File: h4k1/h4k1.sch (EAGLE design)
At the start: 159 parts, among them IC1 STM32F10XCXT6, K1 CHERRY-MX-LED, K10 CHERRY-MX-LED, K11 CHERRY-MX-LED, K12 CHERRY-MX-LED, K13 CHERRY-MX-LED, K14 CHERRY-MX-LED, K15 CHERRY-MX-LED, K16 CHERRY-MX-LED, K17 CHERRY-MX-LED, K18 CHERRY-MX-LED, K19 CHERRY-MX-LED, K2 CHERRY-MX-LED, K20 CHERRY-MX-LED, K21 CHERRY-MX-LED, K22 CHERRY-MX-LED, K23 CHERRY-MX-LED, K24 CHERRY-MX-LED, K25 CHERRY-MX-LED, K26 CHERRY-MX-LED, K27 CHERRY-MX-LED, K28 CHERRY-MX-LED, K29 CHERRY-MX-LED, K3 CHERRY-MX-LED, K30 CHERRY-MX-LED, K31 CHERRY-MX-LED, K32 CHERRY-MX-LED, K33 CHERRY-MX-LED, K34 CHERRY-MX-LED, K35 CHERRY-MX-LED, K36 CHERRY-MX-LED, K37 CHERRY-MX-LED, K38 CHERRY-MX-LED, K39 CHERRY-MX-LED, K4 CHERRY-MX-LED, K40 CHERRY-MX-LED, K41 CHERRY-MX-LED, K42 CHERRY-MX-LED, K43 CHERRY-MX-LED, K44 CHERRY-MX-LED, K45 CHERRY-MX-LED, K46 CHERRY-MX-LED, K47 CHERRY-MX-LED, K48 CHERRY-MX-LED, K49 CHERRY-MX-LED, K5 CHERRY-MX-LED, K50 CHERRY-MX-LED, K51 CHERRY-MX-LED, K52 CHERRY-MX-LED, K53 CHERRY-MX-LED, K54 CHERRY-MX-LED, K55 CHERRY-MX-LED, K56 CHERRY-MX-LED, K57 CHERRY-MX-LED, K58 CHERRY-MX-LED, K59 CHERRY-MX-LED, K6 CHERRY-MX-LED, K60 CHERRY-MX-LED, K61 CHERRY-MX-LED, K62 CHERRY-MX-LED, K63 CHERRY-MX-LED, K64 CHERRY-MX-LED, K7 CHERRY-MX-LED, K8 CHERRY-MX-LED, K9 CHERRY-MX-LED

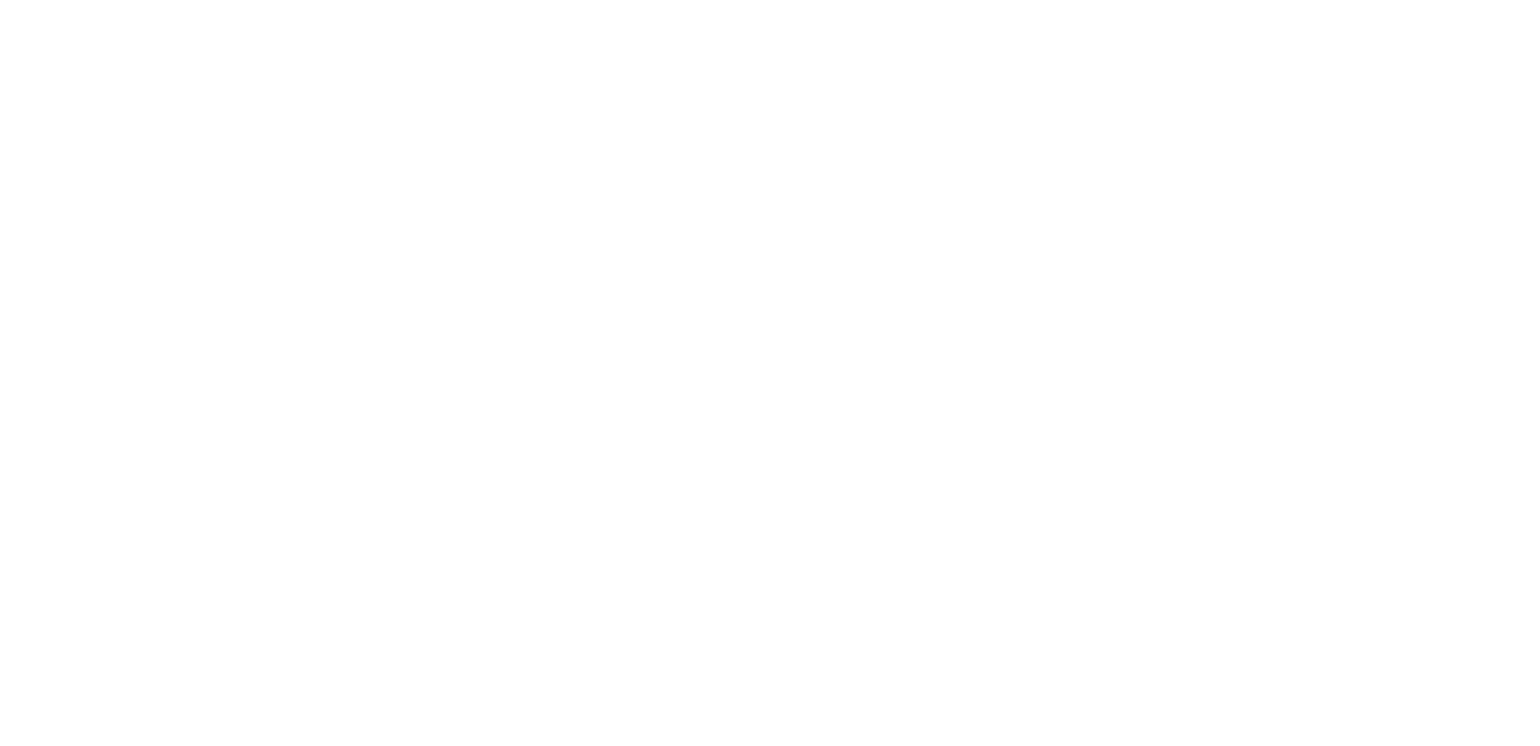
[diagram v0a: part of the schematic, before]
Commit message: add usb hub
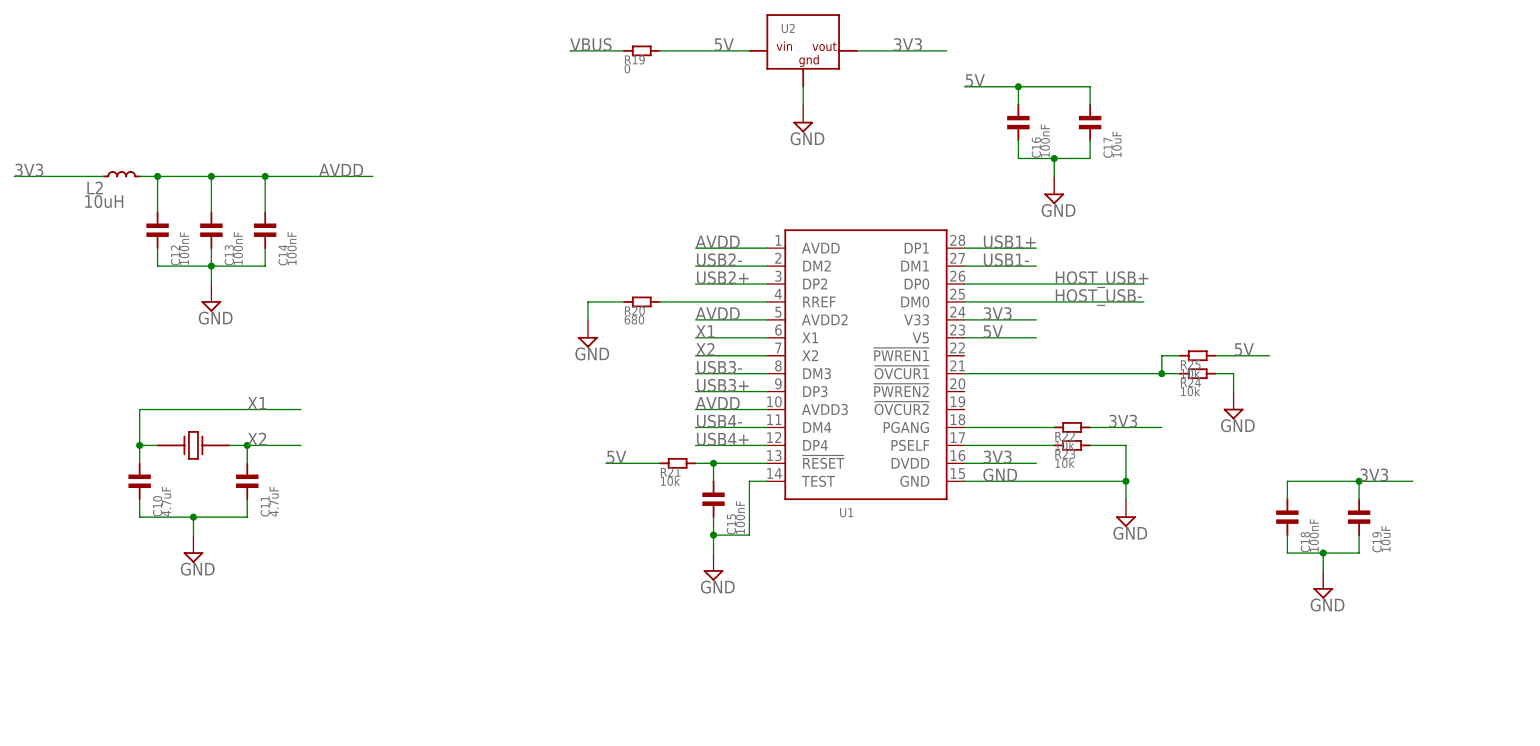
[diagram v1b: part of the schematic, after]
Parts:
- added C10, C11: 4.7uF, hqc-basic:C-0603
- added C12, C13, C14, C15, C16, C18: 100nF, hqc-basic:C-0603
- added C17, C19: 10uF, hqc-basic:C-0603
- added L2: 10uH, hqc-basic:L-0603
- added R19: 0, hqc-basic:R-0603
- added R20: 680, hqc-basic:R-0603
- added R21, R22, R23, R24, R25: 10k, hqc-basic:R-0603
- added U1: G850G, hqc-communication:G850G
- added U2: (no value), hqc-power:AMS1117-33
- added X3: (no value), hqc-crystal:49S-CRYSTAL
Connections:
- new net 3V3: C18.P$2, C19.P$2, L2.P$1, R22.P$2, U1.DVDD, U1.V33, U2.VOUT
- new net 5V: C16.P$2, C17.P$2, R19.P$2, R21.P$1, R25.P$2, U1.V5, U2.VIN
- new net AVDD: C12.P$2, C13.P$2, C14.P$2, L2.P$2, U1.AVDD, U1.AVDD2, U1.AVDD3
- new net HOST_USB+: U1.DP0
- new net HOST_USB-: U1.DM0
- new net N$24: C15.P$2, R21.P$2, U1.!RESET
- new net N$26: R20.P$2, U1.RREF
- new net N$28: R22.P$1, U1.PGANG
- new net N$30: R23.P$1, U1.PSELF
- new net N$34: R24.P$1, R25.P$1, U1.!OVCUR1
- new net USB1+: U1.DP1
- new net USB1-: U1.DM1
- new net USB2+: U1.DP2
- new net USB2-: U1.DM2
- new net USB3+: U1.DP3
- new net USB3-: U1.DM3
- new net USB4+: U1.DP4
- new net USB4-: U1.DM4
- new net VBUS: R19.P$1
- new net X1: C10.P$2, U1.X1, X3.P$1
- new net X2: C11.P$2, U1.X2, X3.P$2
- net GND: now also C10.P$1, C11.P$1, C12.P$1, C13.P$1, C14.P$1, C15.P$1, C16.P$1, C17.P$1, C18.P$1, C19.P$1, R20.P$1, R23.P$2, R24.P$2, U1.GND, U1.TEST, U2.GND

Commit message: audio done
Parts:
- added C20, C21: (no value), hqc:C-0805
- added C22, C23, C24, C25, C26: 1uF, hqc:C-0805
- added C27: 10uF, hqc:CPOL-3216
- added C28, C29: 22nF, hqc:C-0805
- added C30, C31: 100uF, hqc:CPOL-7343
- added C32, C33: 1uF, hqc:CPOL-3216
- added J1: (no value), hqc-connector:PH-5AWD
- added J2: PJ-313D-AUDIO-JACK, hqc:PJ-313D-AUDIO-JACK
- added R26: 1M, hqc:R-0805
- added R27, R28: 1.5k, hqc:R-0805
- added R29, R30: 22, hqc:R-0805
- added R31, R32: 16, hqc:R-0805
- added R33, R34: 330, hqc:R-0805
- added U3: PCM2704CDB, hqc:PCM2704CDB
- added X4: 12M, hqc-crystal:49S-CRYSTAL
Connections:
- new net AUDIO_L: C32.P$1, J2.P$3
- new net AUDIO_R: C33.P$1, J2.P$2
- new net N$32: C20.P$2, R26.P$1, U3.P$1, X4.P$1
- new net N$36: C21.P$1, R26.P$2, U3.P$28, X4.P$2
- new net N$38: R29.P$2, U3.P$8
- new net N$40: R30.P$2, U3.P$9
- new net N$42: C22.P$1, R27.P$1, R28.P$2, U3.P$21, U3.P$25, U3.P$26, U3.P$4, U3.P$7
- new net N$44: C25.P$1, U3.P$20
- new net N$46: C30.P$2, C32.P$2, R33.P$2
- new net N$48: C24.P$1, U3.P$13
- new net N$50: R27.P$2, U3.P$3
- new net N$54: C26.P$1, U3.P$16
- new net N$55: C27.P$1, U3.P$18
- new net N$62: C31.P$2, C33.P$2, R34.P$2
- new net N$64: C29.P$1, R32.P$2
- new net N$66: C28.P$1, R31.P$2
- new net SHIELD: J1.P$5
- new net VOUT_L: C28.P$2, C30.P$1, U3.P$14
- new net VOUT_R: C29.P$2, C31.P$1, U3.P$15
- net GND: now also C20.P$1, C21.P$2, C22.P$2, C23.P$1, C24.P$2, C25.P$2, C26.P$2, C27.P$2, J1.P$4, J2.P$1, R31.P$1, R32.P$1, R33.P$1, R34.P$1, U3.P$11, U3.P$12, U3.P$17, U3.P$19, U3.P$6
- net HOST_USB+: now also J1.P$3
- net HOST_USB-: now also J1.P$2
- net USB1+: now also R28.P$1, R30.P$1
- net USB1-: now also R29.P$1
- net VBUS: now also C23.P$2, J1.P$1, U3.P$10

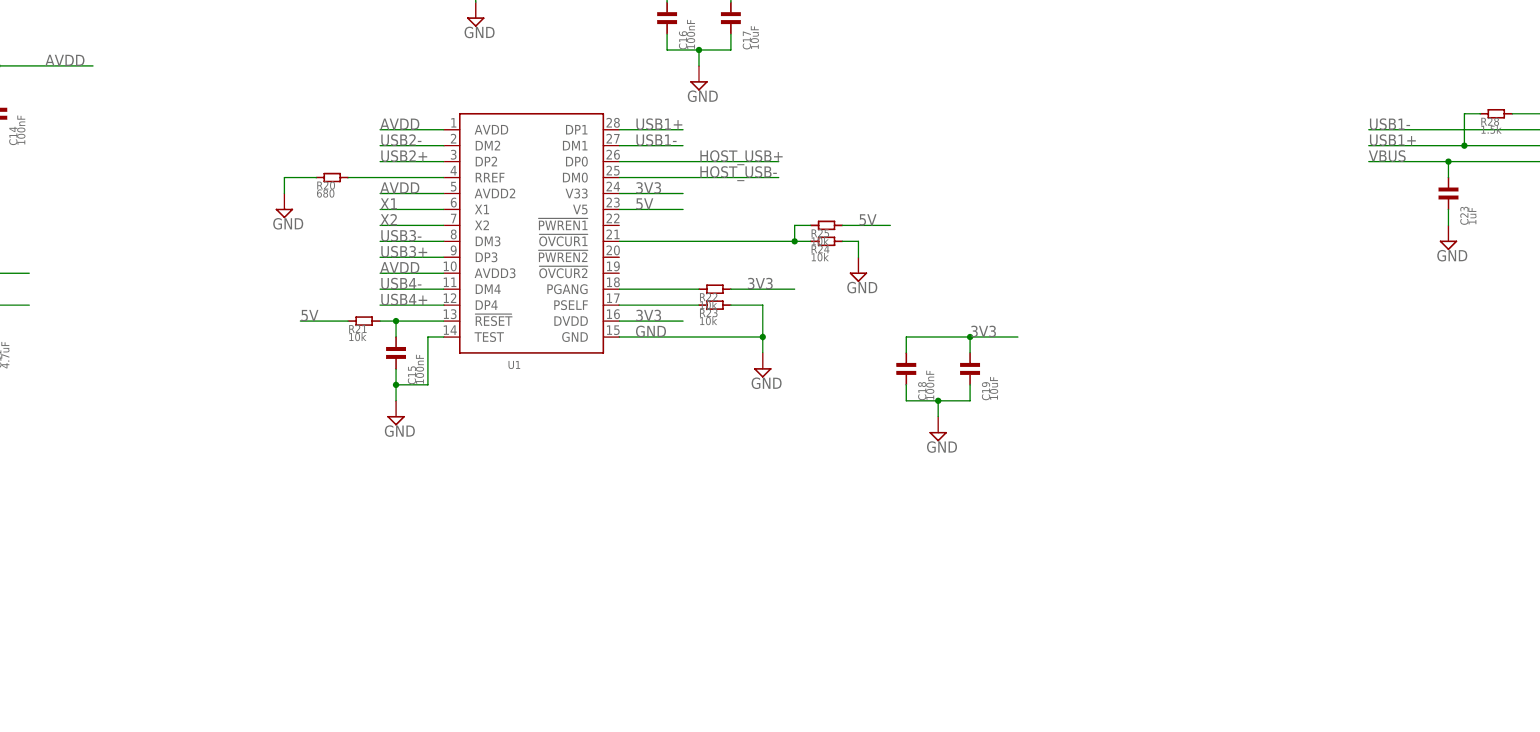
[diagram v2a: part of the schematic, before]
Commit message: add usb connector
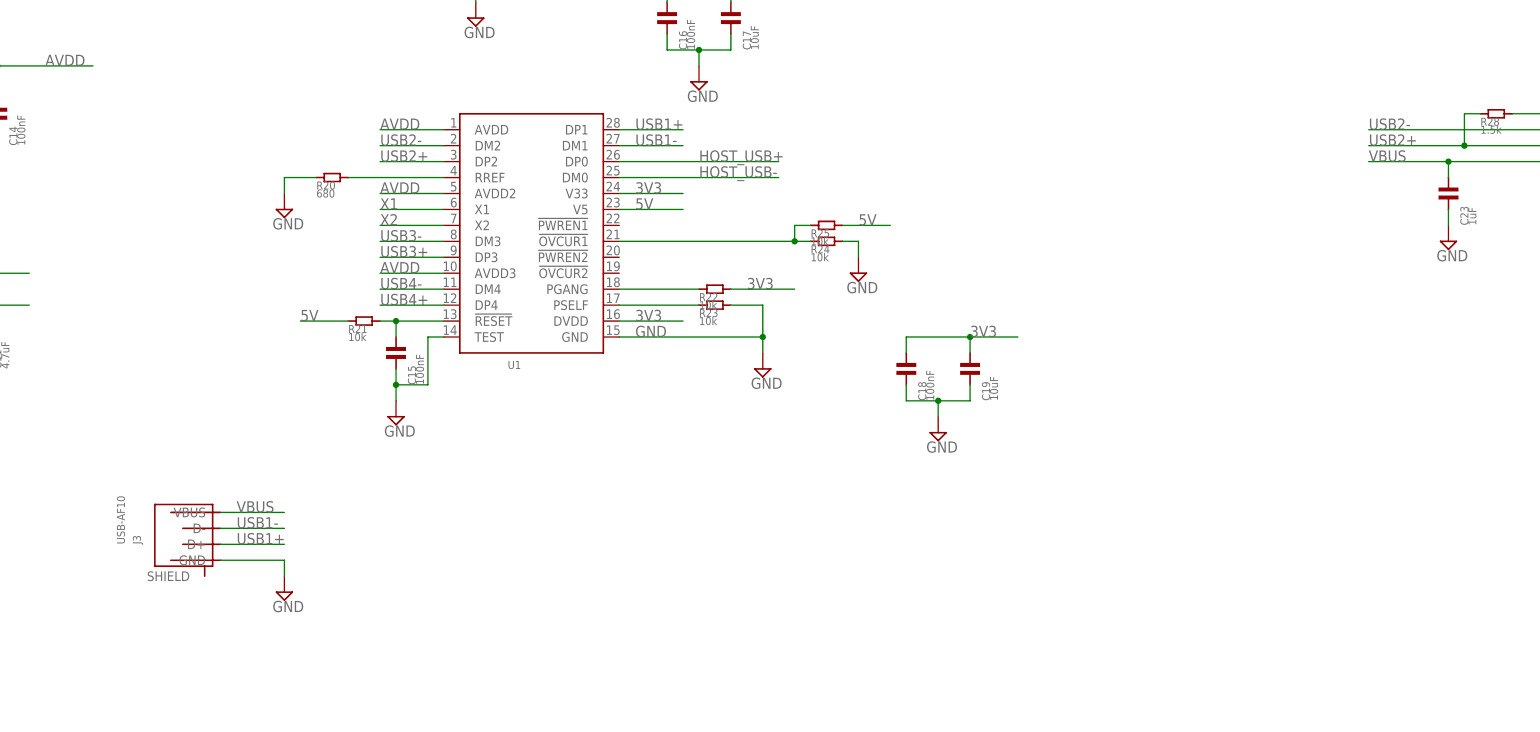
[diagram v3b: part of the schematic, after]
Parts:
- added J3: USB-AF10, hqc:USB-AF10
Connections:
- net GND: now also J3.GND
- net USB1+: now also J3.D+; no longer R28.P$1, R30.P$1
- net USB1-: now also J3.D-; no longer R29.P$1
- net USB2+: now also R28.P$1, R30.P$1
- net USB2-: now also R29.P$1
- net VBUS: now also J3.VBUS
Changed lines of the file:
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@@
 <part name="J2" library="hqc" deviceset="PJ-313D-AUDIO-JACK" device=""/>
 <part name="SUPPLY26" library="supply2" deviceset="GND" device=""/>
+<part name="J3" library="hqc" deviceset="USB-AF10" device=""/>
+<part name="SUPPLY27" library="supply2" deviceset="GND" device=""/>
 </parts>
 <sheets>
@@
 <instance part="J2" gate="G$1" x="373.38" y="238.76"/>
 <instance part="SUPPLY26" gate="GND" x="398.78" y="231.14"/>
+<instance part="J3" gate="G$1" x="10.16" y="160.02"/>
+<instance part="SUPPLY27" gate="GND" x="22.86" y="149.86"/>
 </instances>
 <busses>
@@
 <pinref part="J2" gate="G$1" pin="P$1"/>
 </segment>
+<segment>
+<pinref part="J3" gate="G$1" pin="GND"/>
+<wire x1="12.7" y1="154.94" x2="22.86" y2="154.94" width="0.1524" layer="91"/>
+<wire x1="22.86" y1="154.94" x2="22.86" y2="152.4" width="0.1524" layer="91"/>
+<pinref part="SUPPLY27" gate="GND" pin="GND"/>
+</segment>
 </net>
 <net name="OSC32_1" class="0">
@@
 <junction x="208.28" y="218.44"/>
 </segment>
+<segment>
+<pinref part="J3" gate="G$1" pin="VBUS"/>
+<wire x1="12.7" y1="162.56" x2="22.86" y2="162.56" width="0.1524" layer="91"/>
+<label x="15.24" y="162.56" size="1.778" layer="95"/>
+</segment>
 </net>
 <net name="5V" class="0">
@@
 <label x="38.1" y="220.98" size="1.778" layer="95"/>
 </segment>
+<segment>
+<pinref part="R29" gate="G$1" pin="P$1"/>
+<wire x1="243.84" y1="223.52" x2="195.58" y2="223.52" width="0.1524" layer="91"/>
+<label x="195.58" y="223.52" size="1.778" layer="95"/>
+</segment>
 </net>
 <net name="USB2+" class="0">
@@
 <wire x1="38.1" y1="218.44" x2="48.26" y2="218.44" width="0.1524" layer="91"/>
 <label x="38.1" y="218.44" size="1.778" layer="95"/>
+</segment>
+<segment>
+<pinref part="R30" gate="G$1" pin="P$1"/>
+<wire x1="238.76" y1="220.98" x2="210.82" y2="220.98" width="0.1524" layer="91"/>
+<pinref part="R28" gate="G$1" pin="P$1"/>
+<wire x1="213.36" y1="226.06" x2="210.82" y2="226.06" width="0.1524" layer="91"/>
+<wire x1="210.82" y1="226.06" x2="210.82" y2="220.98" width="0.1524" layer="91"/>
+<junction x="210.82" y="220.98"/>
+<wire x1="210.82" y1="220.98" x2="195.58" y2="220.98" width="0.1524" layer="91"/>
+<label x="195.58" y="220.98" size="1.778" layer="95"/>
 </segment>
 </net>
@@
 </segment>
 <segment>
-<pinref part="R30" gate="G$1" pin="P$1"/>
-<wire x1="238.76" y1="220.98" x2="210.82" y2="220.98" width="0.1524" layer="91"/>
-<pinref part="R28" gate="G$1" pin="P$1"/>
-<wire x1="213.36" y1="226.06" x2="210.82" y2="226.06" width="0.1524" layer="91"/>
-<wire x1="210.82" y1="226.06" x2="210.82" y2="220.98" width="0.1524" layer="91"/>
-<junction x="210.82" y="220.98"/>
-<wire x1="210.82" y1="220.98" x2="195.58" y2="220.98" width="0.1524" layer="91"/>
-<label x="195.58" y="220.98" size="1.778" layer="95"/>
+<pinref part="J3" gate="G$1" pin="D+"/>
+<wire x1="12.7" y1="157.48" x2="22.86" y2="157.48" width="0.1524" layer="91"/>
+<label x="15.24" y="157.48" size="1.778" layer="95"/>
 </segment>
 </net>
@@
 </segment>
 <segment>
-<pinref part="R29" gate="G$1" pin="P$1"/>
-<wire x1="243.84" y1="223.52" x2="195.58" y2="223.52" width="0.1524" layer="91"/>
-<label x="195.58" y="223.52" size="1.778" layer="95"/>
-</segment>
-</net>
+<pinref part="J3" gate="G$1" pin="D-"/>
+<wire x1="12.7" y1="160.02" x2="22.86" y2="160.02" width="0.1524" layer="91"/>
+<label x="15.24" y="160.02" size="1.778" layer="95"/>
+</segment>
+</net>

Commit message: add switches
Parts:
- added C34, C35: 100nF, hqc-basic:C-0603
- added K65, K66: EVQPUL02K, hqc:EVQPUL02K
- added K67: K3-1280S-F2, hqc:K3-1280S-F2
- added R35, R36: 4.7k, hqc-basic:R-0603
- added U$4: BMX055, sensor:BMX055
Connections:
- new net I2C_SCL: IC1PORTB_H.PB8, R35.P$1, U$4.SCX
- new net I2C_SDA: IC1PORTB_H.PB9, R36.P$1, U$4.SDX
- net GND: now also C34.P$1, C35.P$1, U$4.CSB3, U$4.GNDA, U$4.GNDIO, U$4.SDO1, U$4.SDO2
- net VDD: now also C34.P$2, C35.P$2, R35.P$2, R36.P$2, U$4.PS, U$4.VDD, U$4.VDDIO

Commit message: WIP: layout keyboard switches
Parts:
- removed D57, D58, D59, D60, D61, D62, D63, D64: (no value), hqc-basic:IN4148WS-SWITCHING-DIODE
- removed K47, K48, K49, K50, K51, K52, K53, K54, K55, K56, K57, K58, K59, K60, K61, K62, K63, K64: CHERRY-MX-LED, cherrymx:CHERRY-MX-LED
- K1, K10, K2, K20, K21, K22, K3, K33, K34, K35, K36, K37, K38, K39, K4, K40, K41, K42, K43, K44, K45, K46, K5, K6, K7, K8, K9: device cherrymx:CHERRY-MX-LED -> hqc:CHERRY-MX-LED
- K11, K12, K13, K14, K15, K16, K17, K18, K19, K23, K24, K25, K26, K27, K28, K29, K30, K31, K32: value CHERRY-MX-LED -> CHERRY-MX; device cherrymx:CHERRY-MX-LED -> hqc:CHERRY-MX
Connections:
- removed net KB_R8: K57.SW2, K58.SW2, K59.SW2, K60.SW2, K61.SW2, K62.SW2, K63.SW2, K64.SW2
- removed net N$100: D60.P$2, K60.SW1
- removed net N$101: D61.P$2, K61.SW1
- removed net N$102: D62.P$2, K62.SW1
- removed net N$103: D63.P$2, K63.SW1
- removed net N$104: D64.P$2, K64.SW1
- removed net N$85: D47.P$2, K47.SW1
- removed net N$87: D49.P$2, K49.SW1
- removed net N$89: D51.P$2, K51.SW1
- removed net N$91: D52.P$2, K52.SW1
- removed net N$96: D57.P$2, K57.SW1
- removed net N$97: D58.P$2, K58.SW1
- removed net N$98: D59.P$2, K59.SW1
- new net N$68: D47.P$2, K67.P$1
- new net N$70: D49.P$2, K66.P$1
- net KB_R2: now also K11.PIN-2, K12.PIN-2, K13.PIN-2, K14.PIN-2, K15.PIN-2, K16.PIN-2; no longer K11.SW2, K12.SW2, K13.SW2, K14.SW2, K15.SW2, K16.SW2
- net KB_R3: now also K17.PIN-2, K18.PIN-2, K19.PIN-2, K23.PIN-2, K24.PIN-2; no longer K17.SW2, K18.SW2, K19.SW2, K23.SW2, K24.SW2
- net KB_R4: now also K25.PIN-2, K26.PIN-2, K27.PIN-2, K28.PIN-2, K29.PIN-2, K30.PIN-2, K31.PIN-2, K32.PIN-2; no longer K25.SW2, K26.SW2, K27.SW2, K28.SW2, K29.SW2, K30.SW2, K31.SW2, K32.SW2
- net KB_R6: now also K67.P$2; no longer K47.SW2, K48.SW2
- net KB_R7: now also K65.P$2, K66.P$2; no longer K49.SW2, K50.SW2, K51.SW2, K52.SW2, K53.SW2, K54.SW2, K55.SW2, K56.SW2
- net N$11: no longer D60.P$1
- net N$13: no longer D61.P$1
- net N$15: no longer D62.P$1
- net N$17: no longer D63.P$1
- net N$2: no longer D57.P$1
- net N$20: no longer D64.P$1
- net N$22: now also K11.PIN-1; no longer K11.SW1
- net N$23: no longer D59.P$1
- net N$25: now also K12.PIN-1; no longer K12.SW1
- net N$27: now also K13.PIN-1; no longer K13.SW1
- net N$29: now also K14.PIN-1; no longer K14.SW1
- net N$31: now also K15.PIN-1; no longer K15.SW1
- net N$33: now also K16.PIN-1; no longer K16.SW1
- net N$35: now also K17.PIN-1; no longer K17.SW1
- net N$37: now also K18.PIN-1; no longer K18.SW1
- net N$39: now also K19.PIN-1; no longer K19.SW1
- net N$47: now also K23.PIN-1; no longer K23.SW1
- net N$49: now also K24.PIN-1; no longer K24.SW1
- net N$5: no longer D58.P$1
- net N$51: now also K25.PIN-1; no longer K25.SW1
- net N$52: now also K26.PIN-1; no longer K26.SW1
- net N$53: now also K27.PIN-1; no longer K27.SW1
- net N$56: now also K28.PIN-1; no longer K28.SW1
- net N$57: now also K29.PIN-1; no longer K29.SW1
- net N$58: now also K30.PIN-1; no longer K30.SW1
- net N$59: now also K31.PIN-1; no longer K31.SW1
- net N$60: now also K32.PIN-1; no longer K32.SW1
- net N$86: now also K67.P$3; no longer K48.SW1
- net N$88: now also K65.P$1; no longer K50.SW1
- net N$92: no longer K53.SW1
- net N$93: no longer K54.SW1
- net N$94: no longer K55.SW1
- net N$95: no longer K56.SW1
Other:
- moved on the sheet: K65, K66, K67

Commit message: stm32 layout done
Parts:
- added R37, R38: 15, hqc:R-0805
- C1, C10, C11, C12, C13, C14, C15, C16, C17, C18, C19, C2, C3, C34, C35, C4, C7, C8, C9: device hqc-basic:C-0603 -> hqc:C-0805
- C5, C6: value 4.7uF -> 15pF; device hqc-basic:C-0603 -> hqc:C-0805
- K10, K20, K21, K22, K34, K35, K38, K39, K41, K42, K43, K44, K45: value CHERRY-MX-LED -> CHERRY-MX; device hqc:CHERRY-MX-LED -> hqc:CHERRY-MX
- K17, K25: value CHERRY-MX -> CHERRY-MX-LED; device hqc:CHERRY-MX -> hqc:CHERRY-MX-LED
- L1, L2: device hqc-basic:L-0603 -> hqc:L-0805
- R1, R10, R11, R12, R13, R14, R15, R16, R17, R18, R19, R2, R20, R21, R22, R23, R24, R25, R3, R35, R36, R4, R5, R6, R7, R8, R9: device hqc-basic:R-0603 -> hqc:R-0805
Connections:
- new net N$72: IC1PORTA_H.PA11, R37.P$1
- new net N$74: IC1PORTA_H.PA12, R38.P$1
- new net SWDCLK: IC1PORTA_H.PA14
- new net SWDIO: IC1PORTA_H.PA13
- net KB_C1: now also IC1PORTA_L.PA0
- net KB_C2: now also IC1PORTA_L.PA1
- net KB_C3: now also IC1PORTA_L.PA2
- net KB_C4: now also IC1PORTA_L.PA3
- net KB_C5: now also IC1PORTA_L.PA4
- net KB_C6: now also IC1PORTA_L.PA5
- net KB_C7: now also IC1PORTA_L.PA6
- net KB_C8: now also IC1PORTA_L.PA7
- net KB_R1: now also IC1PORTB_L.PB0
- net KB_R2: now also IC1PORTB_L.PB1, K10.PIN-2; no longer K10.SW2
- net KB_R3: now also IC1PORTB_L.PB2, K17.SW2, K20.PIN-2, K21.PIN-2, K22.PIN-2; no longer K17.PIN-2, K20.SW2, K21.SW2, K22.SW2
- net KB_R4: now also IC1PORTB_L.PB3, K25.SW2; no longer K25.PIN-2
- net KB_R5: now also IC1PORTB_L.PB4, K34.PIN-2, K35.PIN-2, K38.PIN-2, K39.PIN-2; no longer K34.SW2, K35.SW2, K38.SW2, K39.SW2
- net KB_R6: now also IC1PORTB_L.PB5, K41.PIN-2, K42.PIN-2, K43.PIN-2, K44.PIN-2, K45.PIN-2; no longer K41.SW2, K42.SW2, K43.SW2, K44.SW2, K45.SW2
- net KB_R7: now also IC1PORTB_L.PB6
- net N$18: now also K10.PIN-1; no longer K10.SW1
- net N$35: now also K17.SW1; no longer K17.PIN-1
- net N$41: now also K20.PIN-1; no longer K20.SW1
- net N$43: now also K21.PIN-1; no longer K21.SW1
- net N$45: now also K22.PIN-1; no longer K22.SW1
- net N$51: now also K25.SW1; no longer K25.PIN-1
- net N$63: now also K34.PIN-1; no longer K34.SW1
- net N$65: now also K35.PIN-1; no longer K35.SW1
- net N$71: now also K38.PIN-1; no longer K38.SW1
- net N$73: now also K39.PIN-1; no longer K39.SW1
- net N$77: now also K41.PIN-1; no longer K41.SW1
- net N$78: now also K42.PIN-1; no longer K42.SW1
- net N$79: now also K43.PIN-1; no longer K43.SW1
- net N$82: now also K44.PIN-1; no longer K44.SW1
- net N$83: now also K45.PIN-1; no longer K45.SW1
- net USB3+: now also R38.P$2
- net USB3-: now also R37.P$2
